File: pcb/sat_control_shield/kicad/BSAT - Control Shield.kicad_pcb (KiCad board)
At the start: 2 copper layers, 77 x 77 mm, 20 parts, among them P1 POWER, U1 ARDUINO_NANO_V3.0, U2 74HC4052E

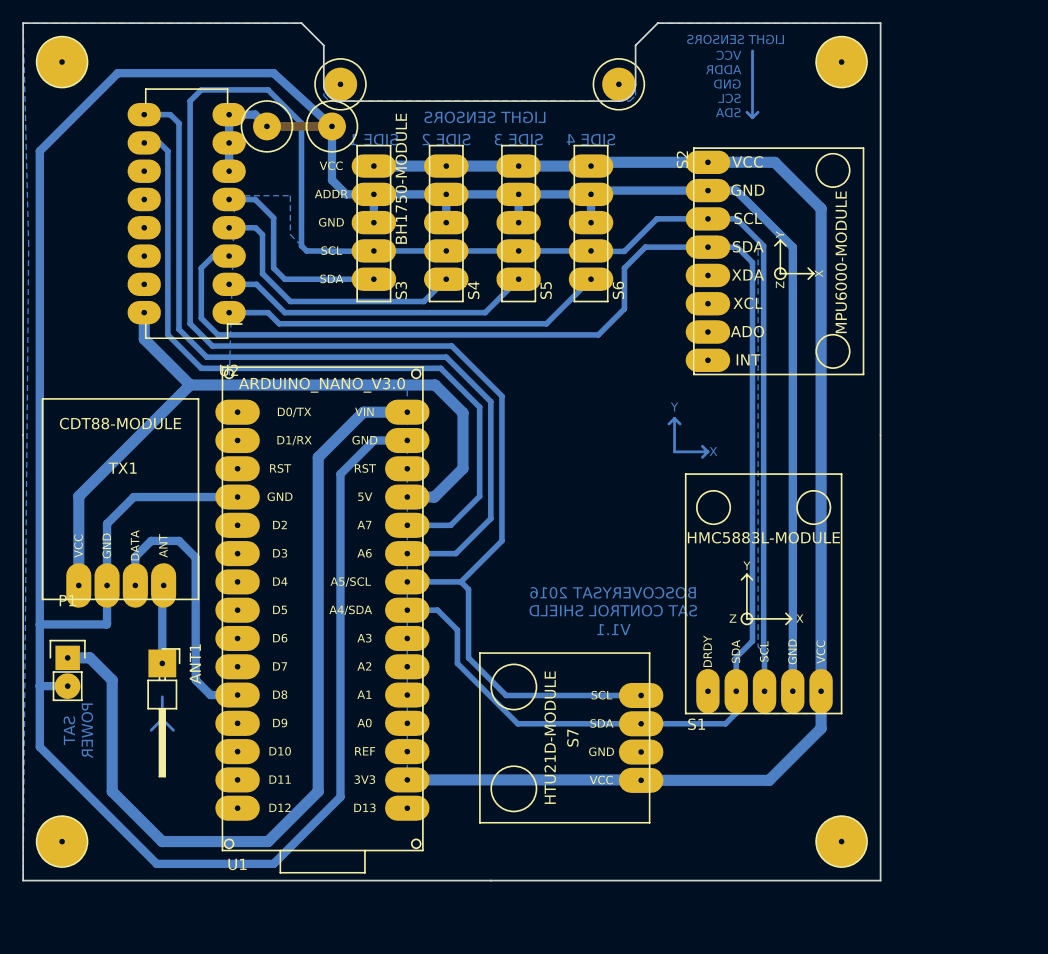
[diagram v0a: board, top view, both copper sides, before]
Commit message: refactor(control-shield): Rediseñar el diagrama de pistas para obtener una placa de doble cara.
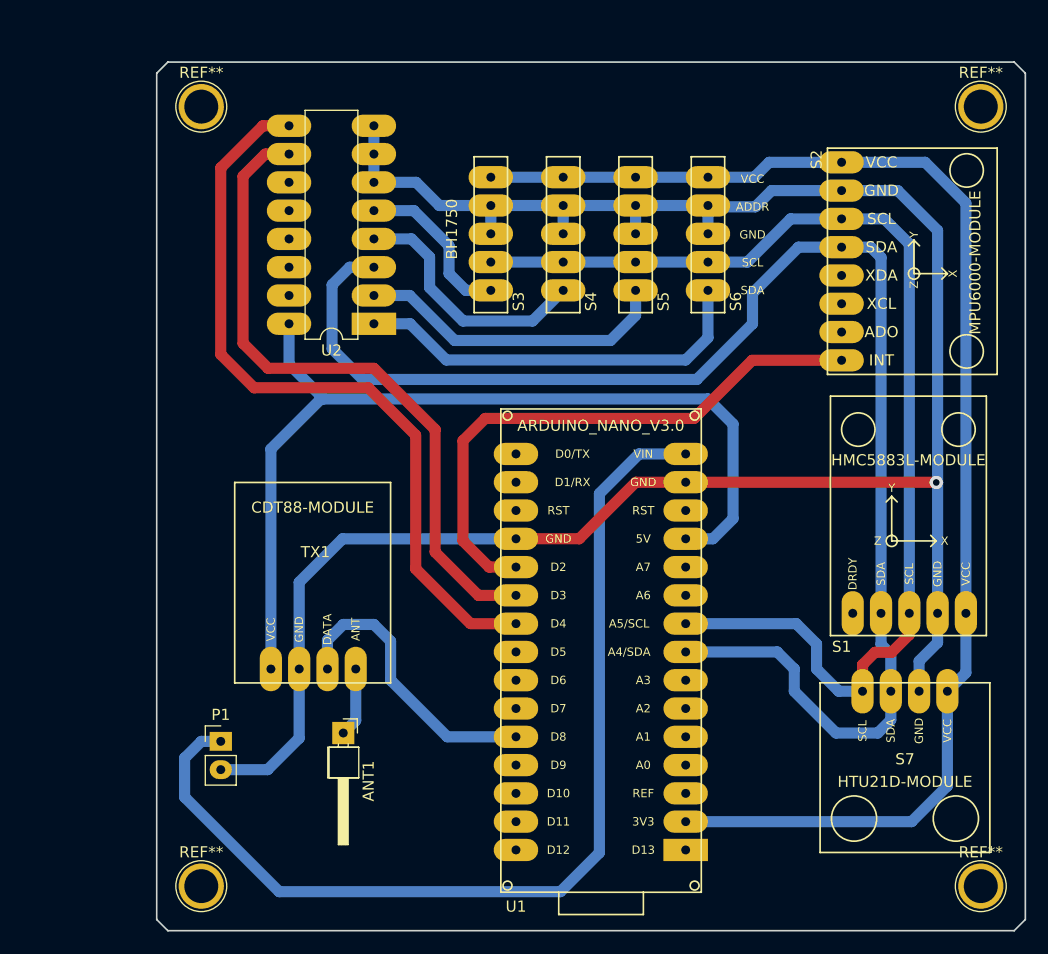
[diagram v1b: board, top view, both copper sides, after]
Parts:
- removed the REF** at (138.2, 54.3)
- removed the REF** at (139.0, 50.5)
- removed the REF** at (114.0, 118.5)
- removed the REF** at (114.0, 48.5)
- removed the REF** at (184.0, 48.5)
- removed the REF** at (184.0, 118.5)
- removed the REF** at (164.0, 50.5)
- removed the REF** at (132.4, 54.3)
- added REF**: 1pin, Connect:1pin, F.Cu at (196.5, 122.5)
- added REF**: 1pin, Connect:1pin, F.Cu at (196.5, 52.5)
- added REF**: 1pin, Connect:1pin, F.Cu at (126.5, 52.5)
- added REF**: 1pin, Connect:1pin, F.Cu at (126.5, 122.5)
- ANT1: footprint Pin_Headers:Pin_Header_Angled_1x01 -> Pin_Headers:Pin_Header_Angled_1x01_Pitch2.54mm
- P1: footprint Pin_Headers:Pin_Header_Straight_1x02 -> Pin_Headers:Pin_Header_Straight_1x02_Pitch2.54mm
- S3: value BH1750-MODULE -> BH1750
- S4, S5, S6: value BH1750-MODULE -> (none)
- moved S7 28.6 mm to (193.5, 105.0), turned to 180 degrees
- moved U1 25.3 mm to (170.0, 119.2)
- moved TX1 18.8 mm to (132.8, 103.0)
- moved ANT1 17.4 mm to (139.2, 108.8)
- moved P1 15.7 mm to (128.2, 109.5)
- moved S1 14.8 mm to (185.0, 98.0)
- moved U2 13.0 mm to (142.0, 72.0)
- moved S2 12.0 mm to (184.0, 57.5)
- moved S3 10.5 mm to (152.5, 69.0)
- moved S4 10.5 mm to (159.0, 69.0)
- moved S5 10.5 mm to (165.5, 69.0)
- moved S6 10.5 mm to (172.0, 69.0)
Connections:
- S2 pad 8: Net-(S2-Pad8) -> /GYRO_INT
- U1 pad 10: /LS_SELECT_1 -> Net-(U1-Pad10)
- U1 pad 11: /LS_SELECT_0 -> Net-(U1-Pad11)
- U1 pad 20: Net-(U1-Pad20) -> /GYRO_INT
- U1 pad 21: Net-(U1-Pad21) -> /LS_SELECT_0
- U1 pad 22: Net-(U1-Pad22) -> /LS_SELECT_1
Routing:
- net GNDREF: track 298.7 -> 194.4 mm, vias 2 -> 1
- net /SCL: track 204.8 -> 102.6 mm
- net /GYRO_INT: track 0.00 -> 51.7 mm
- net (no net): track 23.1 -> 0.00 mm
- net +5V: track 66.9 -> 85.5 mm
- net VCC: track 76.7 -> 91.1 mm
- net /SDA: track 142.3 -> 132.5 mm
- net +3V3: track 127.8 -> 122.6 mm
- net /LS_SELECT_0: track 65.3 -> 60.3 mm
- net /LS_SELECT_1: track 72.6 -> 68.0 mm
- net /SDA_LS_SIDE1: track 18.6 -> 14.9 mm
- net /SDA_LS_SIDE2: track 25.1 -> 22.8 mm
- net /SDA_LS_SIDE4: track 34.6 -> 36.4 mm
- removed copper zone on B.Cu, net (none)
- removed copper zone on B.Cu, net GNDREF
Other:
- board size 77 x 77 mm -> 78 x 78 mm
- net class 0.50 removed
- net class 0.75 removed
- net class 0.80 removed
- net class Default: clearance 0.2 -> 0.5; trace_width 0.25 -> 1; via_dia 0.6 -> 1.2; via_drill 0.4 -> 0.6
- net class Normal removed
- rule trace_clearance: 0.2 -> 0.5
- board text added: "ADDR"
- board text added: "BOSCOVERY SAT CONTROL SHIELD V1.1.3 - FEB 17"
- board text added: "GND"
- board text added: "S1"
- board text added: "S2"
- board text added: "S3"
- board text added: "S4"
- board text added: "SCL"
- board text added: "SDA"
- board text added: "VCC"
- board text added: "Z"
- board text removed: "BOSCOVERYSAT 2016 SAT CONTROL SHIELD"
- board text removed: "SAT POWER"
- board text removed: "SIDE 1"
- board text removed: "SIDE 2"
- board text removed: "SIDE 3"
- board text removed: "SIDE 4"
- board text removed: "V1.1"
- board text removed: "VCC ADDR GND SCL SDA"
